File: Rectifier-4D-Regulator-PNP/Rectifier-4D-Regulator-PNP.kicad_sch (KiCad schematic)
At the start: 15 parts, among them Q1 PNP, U1 LM317_TO-220

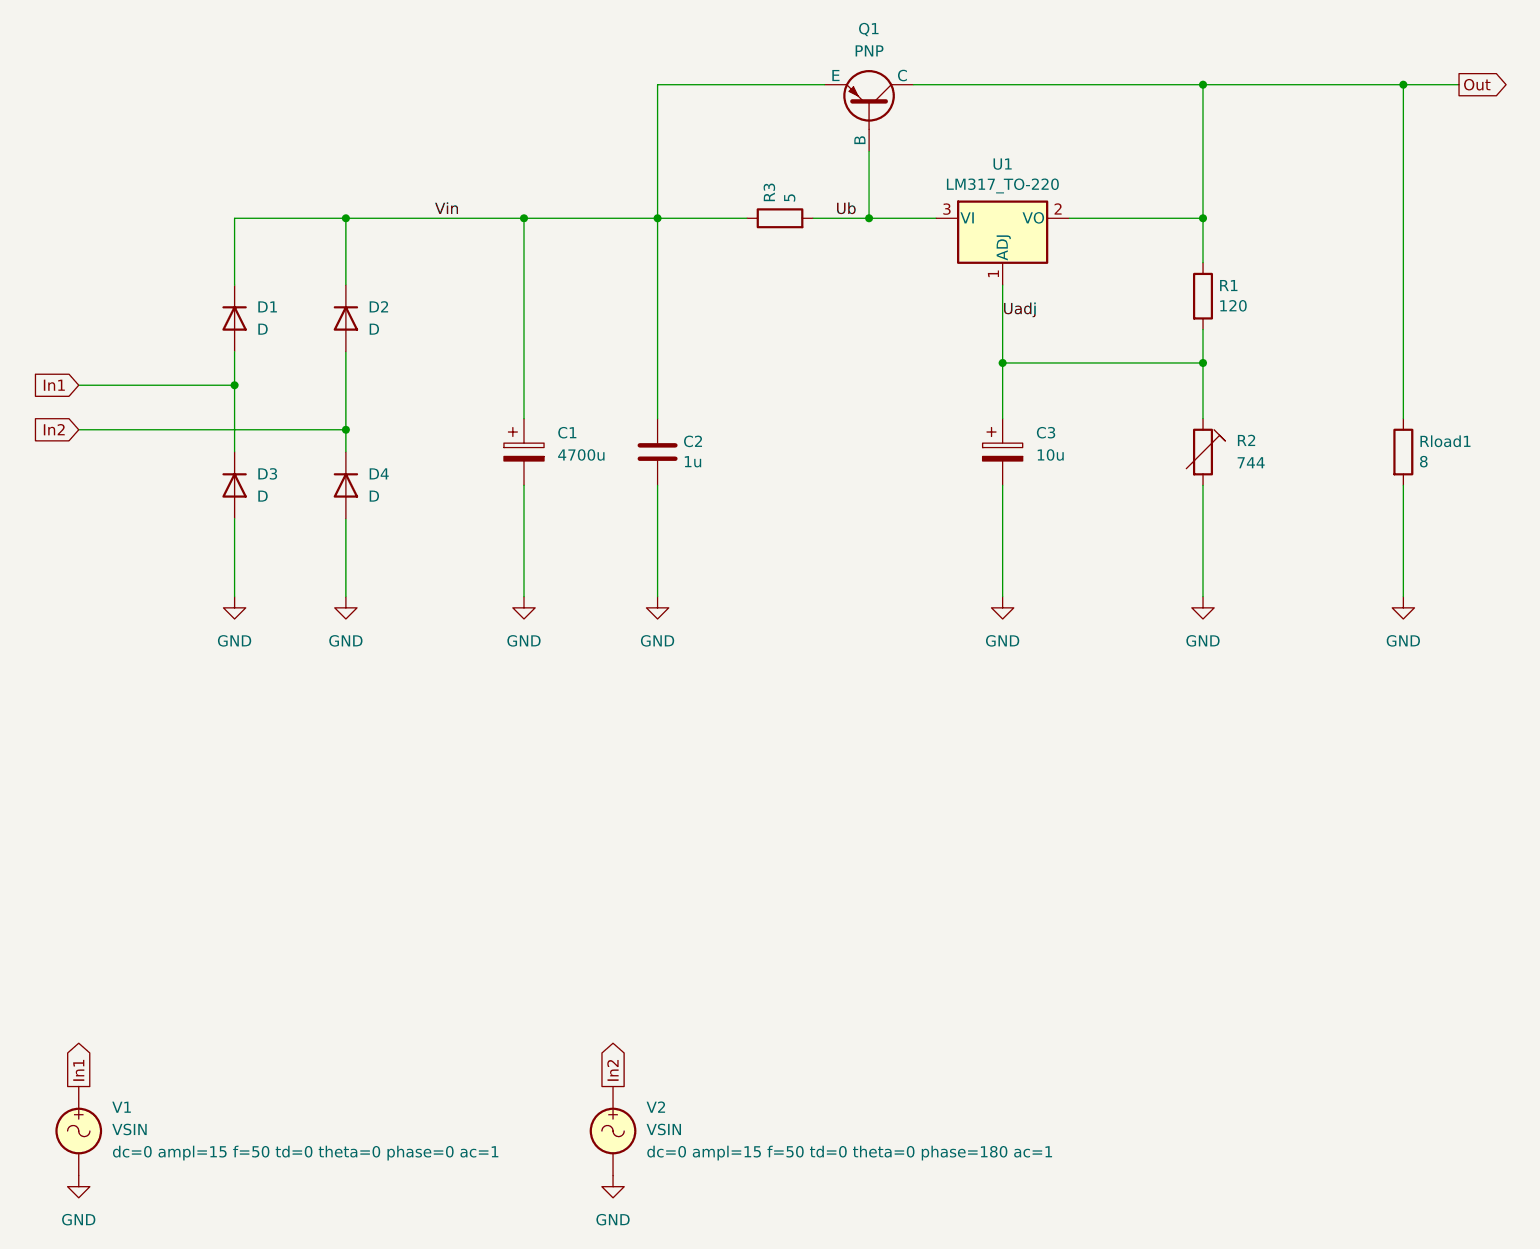
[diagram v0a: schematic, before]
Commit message: Tested/updated for KiCad 9
Schematics are tested and updated for KiCad 9, no changes in circuitry
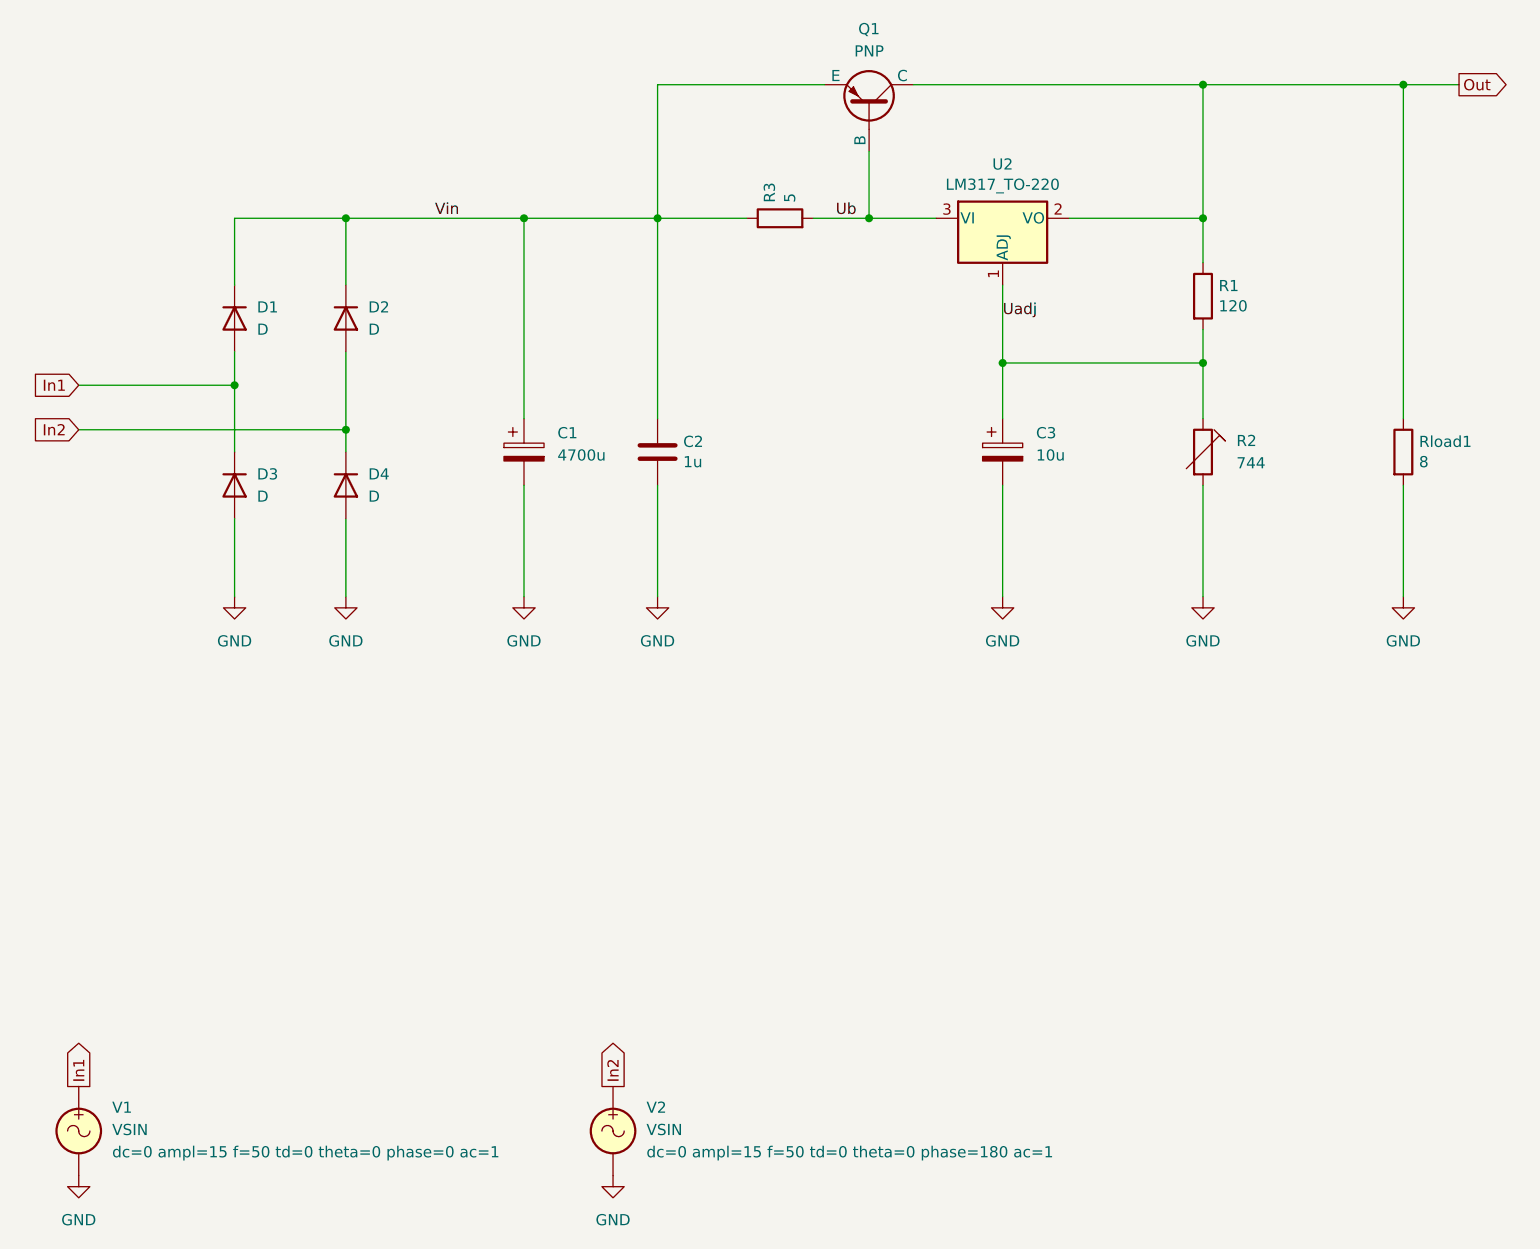
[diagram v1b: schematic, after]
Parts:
- renumbered U1 to U2
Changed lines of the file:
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@@
 (kicad_sch
-	(version 20231120)
+	(version 20250114)
 	(generator "eeschema")
-	(generator_version "8.0")
+	(generator_version "9.0")
 	(paper "A4")
 	(title_block
 		(title "Rectifier with 4 diodes, regulator and PNP passtransistor")
-		(date "2024-12-15")
+		(date "2025-09-13")
 		(company "GitHub/OJStuff")
 	)
@@
 	(label "Vin"
 		(at 97.79 77.47 0)
-		(fields_autoplaced yes)
 		(effects
 			(font
@@
 	(label "Ub"
 		(at 143.51 77.47 0)
-		(fields_autoplaced yes)
 		(effects
 			(font
@@
 	(label "Uadj"
 		(at 162.56 88.9 0)
-		(fields_autoplaced yes)
 		(effects
 			(font
@@
 		(on_board yes)
 		(dnp no)
-		(property "Reference" "U1"
+		(property "Reference" "U2"
 			(at 162.56 71.3232 0)
 			(effects
@@
 		)
 	)
+	(embedded_fonts no)
 )
